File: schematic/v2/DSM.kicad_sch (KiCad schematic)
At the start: 1 part, among them U17 NUCLEO-H753ZI

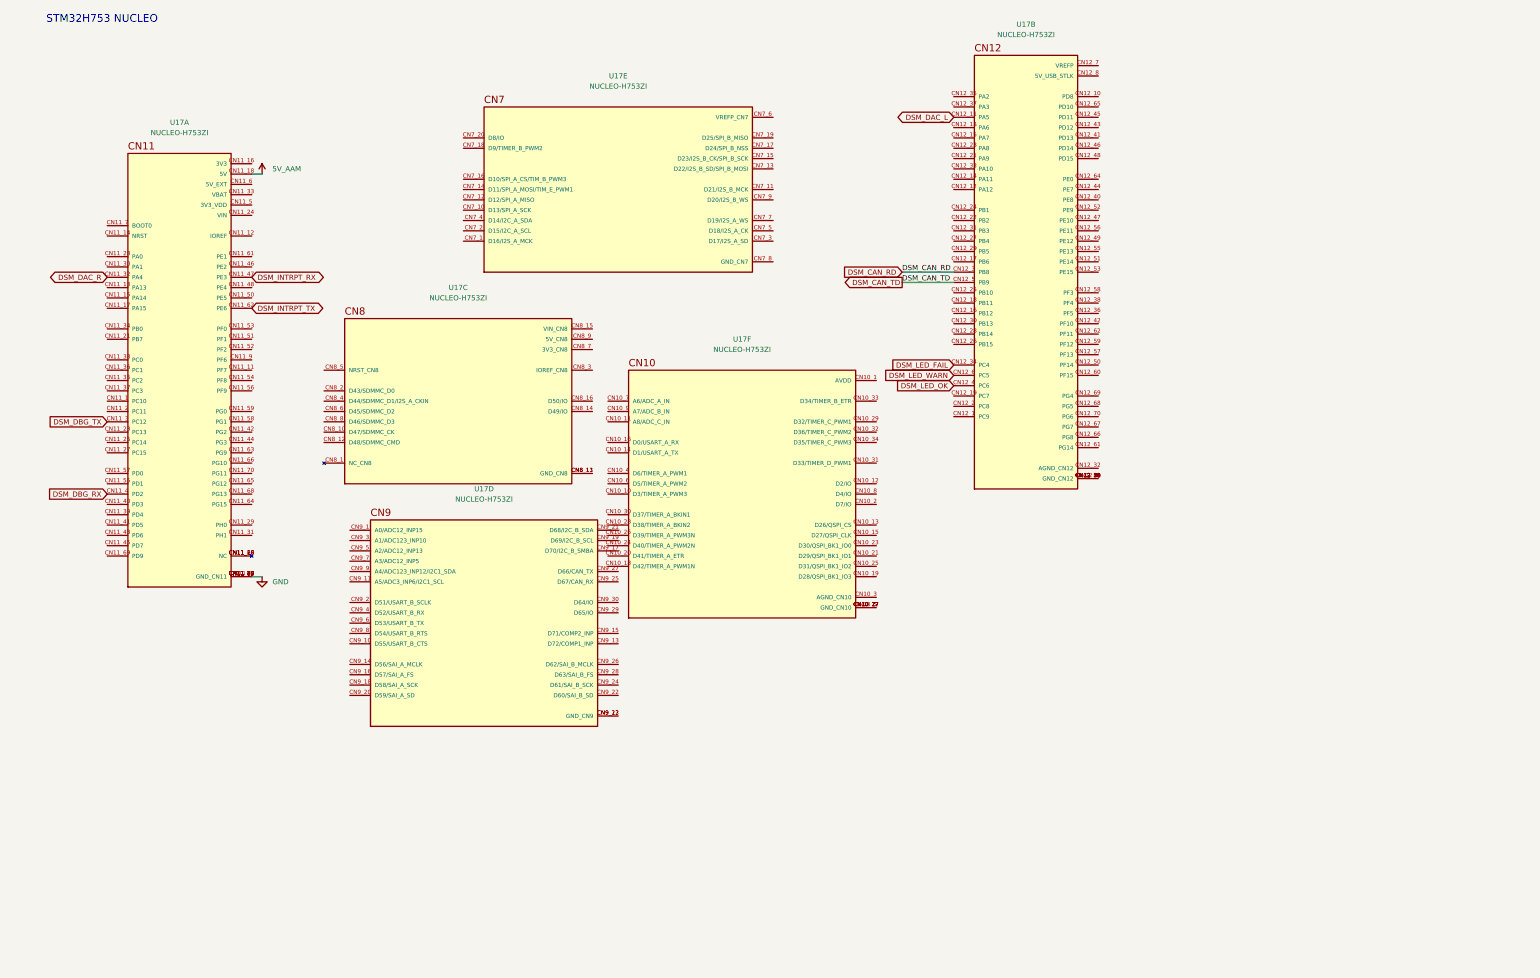
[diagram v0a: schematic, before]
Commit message: moving to multiple sheets for the schematic
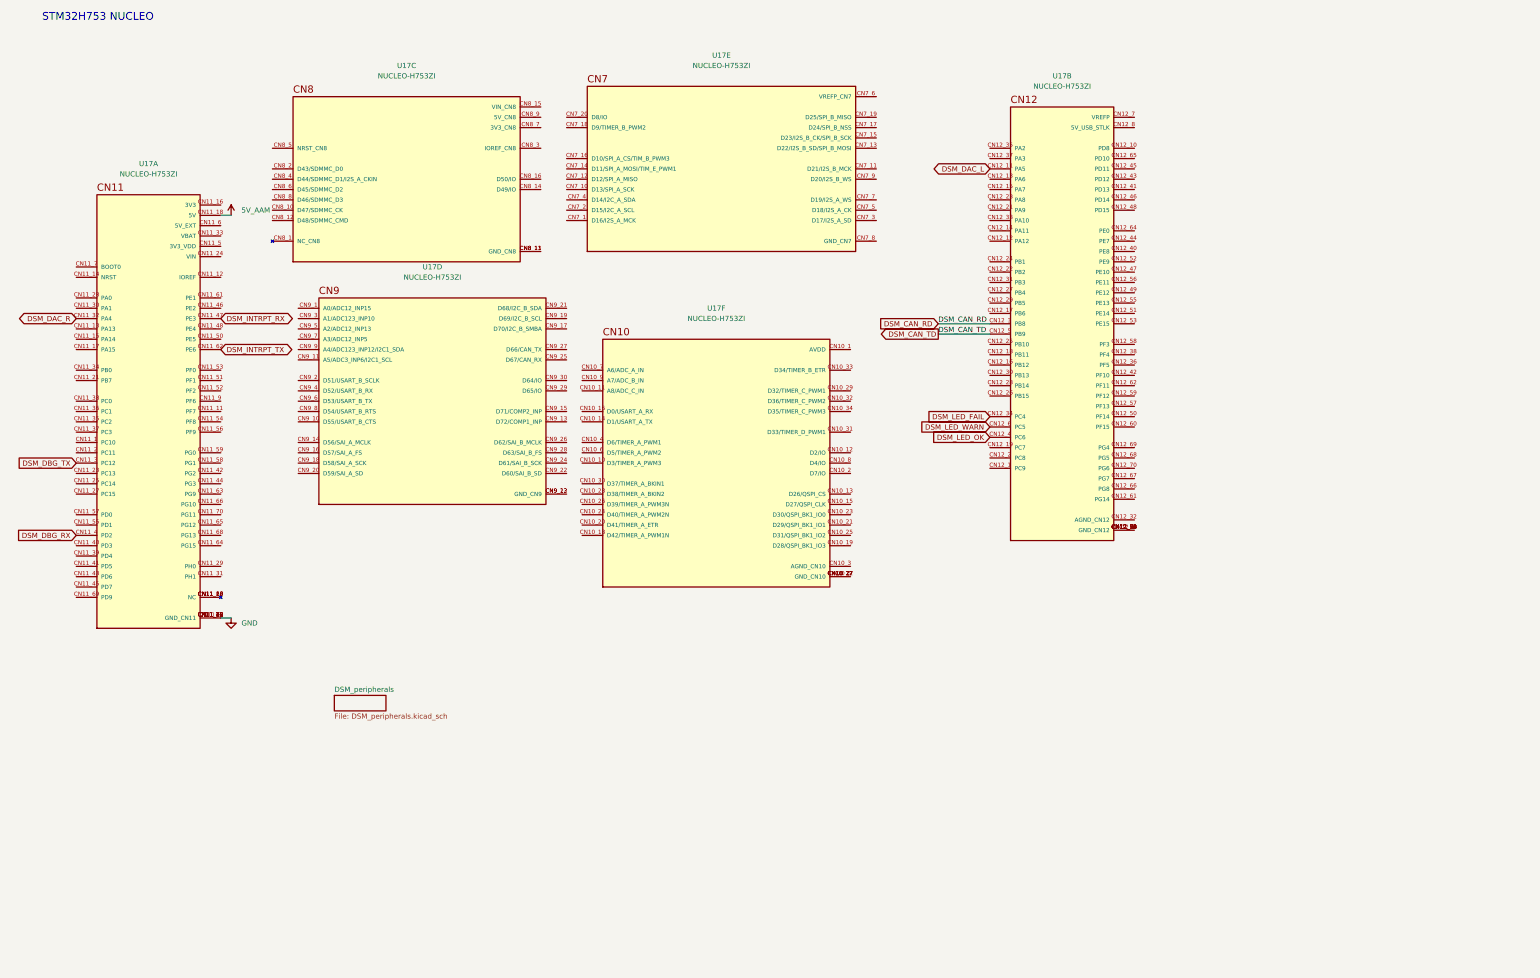
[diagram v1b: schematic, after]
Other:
- added sheet DSM_peripherals (DSM_peripherals.kicad_sch)
- moved on the sheet: U17A, U17B, U17C, U17D, U17E, U17F

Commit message: adding more sheets in the schematic
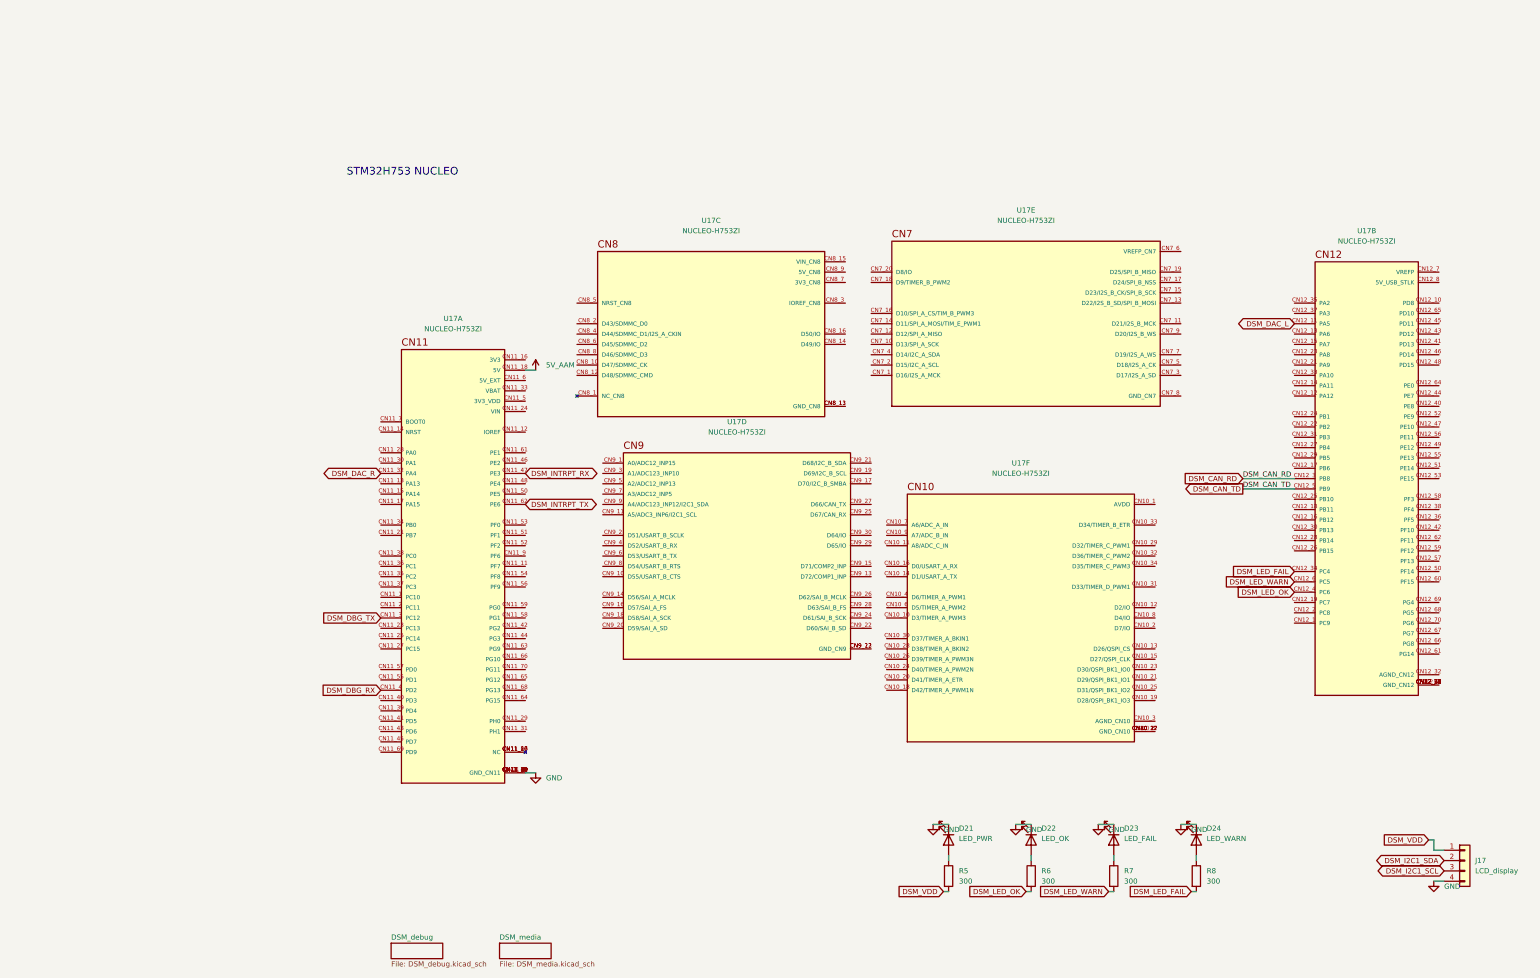
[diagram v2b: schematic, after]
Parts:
- added D21: LED_PWR, LED_SMD:LED_0603_1608Metric, symbol Device:LED
- added D22: LED_OK, LED_SMD:LED_0603_1608Metric, symbol Device:LED
- added D23: LED_FAIL, LED_SMD:LED_0603_1608Metric, symbol Device:LED
- added D24: LED_WARN, LED_SMD:LED_0603_1608Metric, symbol Device:LED
- added J17: LCD_display, Connector_PinHeader_1.00mm:PinHeader_1x04_P1.00mm_Vertical_SMD_Pin1Left, symbol Connector_Generic:Conn_01x04
- added R5, R6, R7, R8: 300, Resistor_SMD:R_0805_2012Metric_Pad1.20x1.40mm_HandSolder, symbol Device:R
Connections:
- net DSM_LED_FAIL: now also R8.2
- net DSM_LED_OK: now also R6.2
- net DSM_LED_WARN: now also R7.2
- net GND: now also D21.1 (K), D22.1 (K), D23.1 (K), D24.1 (K), J17.4 (Pin_4)
- new net: D21.2 (A), R5.1
- new net: D22.2 (A), R6.1
- new net: D24.2 (A), R8.1
- new net: D23.2 (A), R7.1
- new net DSM_I2C1_SCL: J17.3 (Pin_3)
- new net DSM_I2C1_SDA: J17.2 (Pin_2)
- new net DSM_VDD: J17.1 (Pin_1), R5.2
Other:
- removed sheet DSM_peripherals
- added sheet DSM_debug (DSM_debug.kicad_sch)
- added sheet DSM_media (DSM_media.kicad_sch)
- moved on the sheet: U17A, U17B, U17C, U17D, U17E, U17F

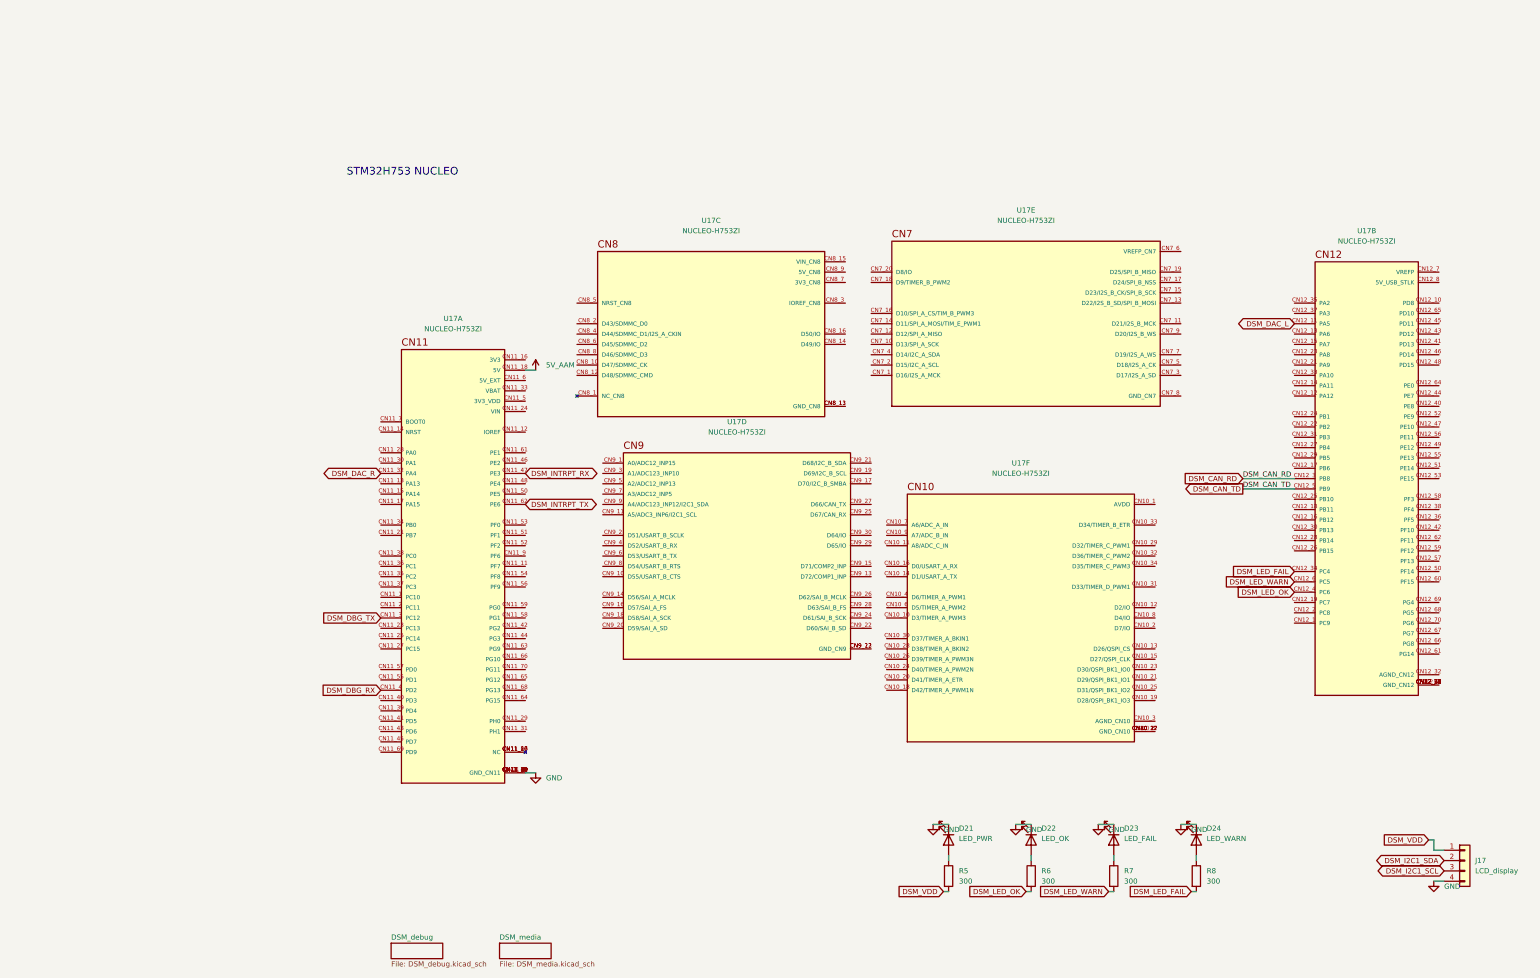
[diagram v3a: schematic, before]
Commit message: v2 updates. remove sniffer
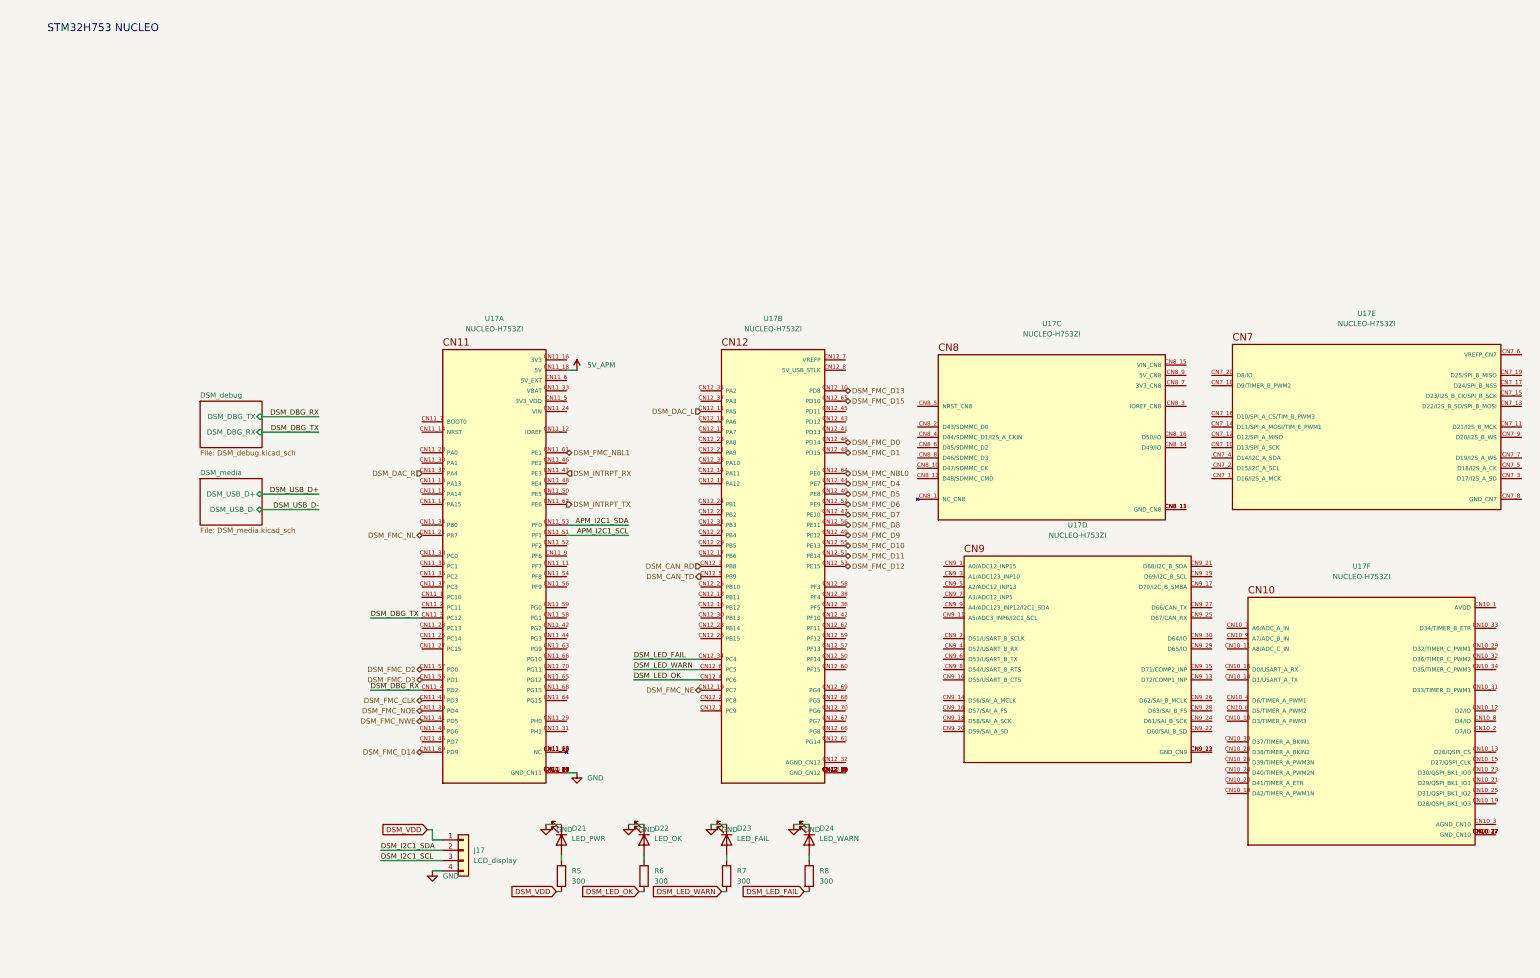
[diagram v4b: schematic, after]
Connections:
- net DSM_FMC_NL: now reaches U17.CN11_21 (PB7)
- net DSM_FMC_NOE: now reaches U17.CN11_39 (PD4)
- net DSM_FMC_CLK: now reaches U17.CN11_40 (PD3)
- net DSM_FMC_NWE: now reaches U17.CN11_41 (PD5)
- net APM_I2C1_SCL: now reaches U17.CN11_51 (PF1)
- net APM_I2C1_SDA: now reaches U17.CN11_53 (PF0)
- net DSM_FMC_D3: now reaches U17.CN11_55 (PD1)
- net DSM_FMC_D2: now reaches U17.CN11_57 (PD0)
- net DSM_FMC_NBL1: now reaches U17.CN11_61 (PE1)
- net DSM_FMC_D14: now reaches U17.CN11_69 (PD9)
- net DSM_FMC_D13: now reaches U17.CN12_10 (PD8)
- net DSM_FMC_NE: now reaches U17.CN12_19 (PC7)
- net DSM_FMC_D5: now reaches U17.CN12_40 (PE8)
- net DSM_FMC_D4: now reaches U17.CN12_44 (PE7)
- net DSM_FMC_D0: now reaches U17.CN12_46 (PD14)
- net DSM_FMC_D7: now reaches U17.CN12_47 (PE10)
- net DSM_FMC_D1: now reaches U17.CN12_48 (PD15)
- net DSM_FMC_D9: now reaches U17.CN12_49 (PE12)
- net DSM_FMC_D11: now reaches U17.CN12_51 (PE14)
- net DSM_FMC_D6: now reaches U17.CN12_52 (PE9)
- net DSM_FMC_D12: now reaches U17.CN12_53 (PE15)
- net DSM_FMC_D10: now reaches U17.CN12_55 (PE13)
- net DSM_FMC_D8: now reaches U17.CN12_56 (PE11)
- net DSM_FMC_NBL0: now reaches U17.CN12_64 (PE0)
- net DSM_FMC_D15: now reaches U17.CN12_65 (PD10)
- net 5V_AAM renamed 5V_APM
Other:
- sheet DSM_debug ports: added DSM_DBG_RX, DSM_DBG_TX; removed none
- sheet DSM_media ports: added DSM_USB_D+, DSM_USB_D-; removed none
- moved on the sheet: D21, D22, D23, D24, J17, R5, R6, R7, R8, U17A, U17B, U17C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

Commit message: no errors in the ERC!
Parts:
- removed unit 5 of U17
- removed unit 3 of U17
- removed unit 6 of U17
- removed unit 4 of U17
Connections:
- net APM_I2C1_SCL is gone; now on net DSM_I2C1_SCL: U17.CN11_51 (PF1)
- net APM_I2C1_SDA is gone; now on net DSM_I2C1_SDA: U17.CN11_53 (PF0)
- net DSM_USB_D+: now also U17.CN12_14 (PA11)
- net DSM_USB_D-: now also U17.CN12_12 (PA12)
- net GND: now also U17.CN12_20 (GND_CN12), U17.CN12_39 (GND_CN12), U17.CN12_54 (GND_CN12), U17.CN12_63 (GND_CN12), U17.CN12_71 (GND_CN12), U17.CN12_72 (GND_CN12), U17.CN12_9 (GND_CN12)
- no-connect marks 0 -> 10

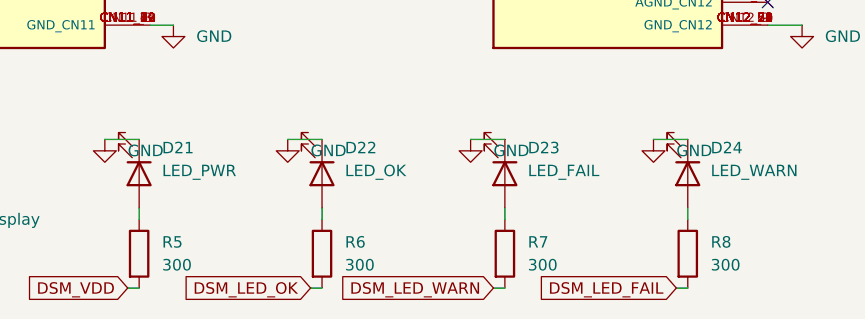
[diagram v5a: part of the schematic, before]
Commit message: need to update PCB and new traces
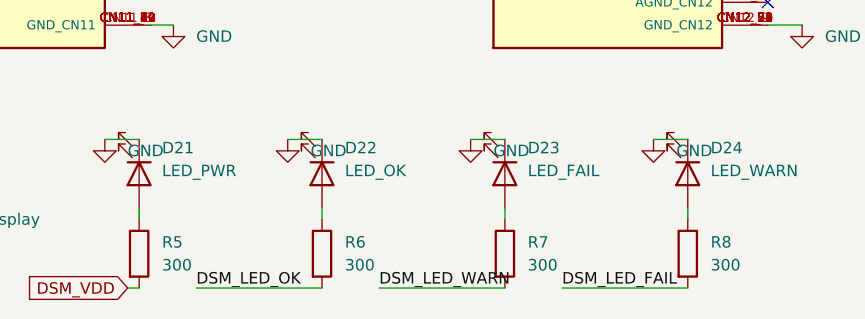
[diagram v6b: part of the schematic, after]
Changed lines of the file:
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@@
 	(wire
 		(pts
-			(xy 181.61 231.14) (xy 182.88 231.14)
+			(xy 168.91 231.14) (xy 182.88 231.14)
 		)
 		(stroke
@@
 	(wire
 		(pts
-			(xy 161.29 231.14) (xy 162.56 231.14)
+			(xy 148.59 231.14) (xy 162.56 231.14)
 		)
 		(stroke
@@
 	(wire
 		(pts
-			(xy 201.93 231.14) (xy 203.2 231.14)
+			(xy 189.23 231.14) (xy 203.2 231.14)
 		)
 		(stroke
@@
 		)
 	)
+	(label "DSM_LED_OK"
+		(at 148.59 231.14 0)
+		(effects
+			(font
+				(size 1.27 1.27)
+			)
+			(justify left bottom)
+		)
+	)
 	(label "DSM_I2C1_SCL"
 		(at 158.75 143.51 180)
@@
 		)
 	)
+	(label "DSM_LED_WARN"
+		(at 168.91 231.14 0)
+		(effects
+			(font
+				(size 1.27 1.27)
+			)
+			(justify left bottom)
+		)
+	)
 	(label "DSM_I2C1_SDA"
 		(at 97.79 220.98 0)
@@
 			)
 			(justify right bottom)
+		)
+	)
+	(label "DSM_LED_FAIL"
+		(at 189.23 231.14 0)
+		(effects
+			(font
+				(size 1.27 1.27)
+			)
+			(justify left bottom)
 		)
 	)
@@
 		)
 	)
-	(global_label "DSM_LED_FAIL"
-		(shape input)
-		(at 201.93 231.14 180)
-		(fields_autoplaced yes)
-		(effects
-			(font
-				(size 1.27 1.27)
-			)
-			(justify right)
-		)
-		(property "Intersheetrefs" "${INTERSHEET_REFS}"
-			(at 185.8215 231.14 0)
-			(effects
-				(font
-					(size 1.27 1.27)
-				)
-				(justify right)
-				(hide yes)
-			)
-		)
-	)
 	(global_label "DSM_VDD"
 		(shape input)
@@
 			(effects
 				(font
-					(size 1.27 1.27)
-				)
-				(justify right)
-				(hide yes)
-			)
-		)
-	)
-	(global_label "DSM_LED_OK"
-		(shape input)
-		(at 161.29 231.14 180)
-		(fields_autoplaced yes)
-		(effects
-			(font
-				(size 1.27 1.27)
-			)
-			(justify right)
-		)
-		(property "Intersheetrefs" "${INTERSHEET_REFS}"
-			(at 146.3911 231.14 0)
-			(effects
-				(font
-					(size 1.27 1.27)
-				)
-				(justify right)
-				(hide yes)
-			)
-		)
-	)
-	(global_label "DSM_LED_WARN"
-		(shape input)
-		(at 181.61 231.14 180)
-		(fields_autoplaced yes)
-		(effects
-			(font
-				(size 1.27 1.27)
-			)
-			(justify right)
-		)
-		(property "Intersheetrefs" "${INTERSHEET_REFS}"
-			(at 164.1711 231.14 0)
-			(effects
-				(font
